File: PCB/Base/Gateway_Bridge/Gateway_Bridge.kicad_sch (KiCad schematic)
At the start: 57 parts, among them J1 J_DIAG, J2 J_I2C2, J3 STM32_Breakout, J5 J_CAN_TERM, J6 J_I2C1, J7 J_SWD, J8 J_BUS_IN, J9 J_BUS_OUT, SW1 RESET, U1 STM32F103C8Tx, U2 SN65HVD230, U3 AMS1117-3.3, U4 RP2040-ZERO, Y1 8MHz

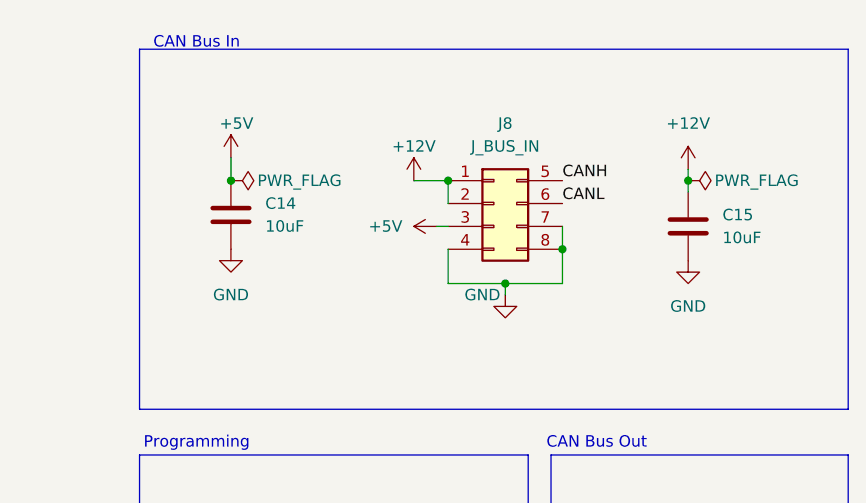
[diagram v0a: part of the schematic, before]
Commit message: feat(pcb): input-rail TVS + AO3400A backlight FET + 35V bus cap on base boards
Roll the #214 input-rail TVS fleet standard into both base boards, plus
two margin upgrades folded into the same rev:

- Input-rail TVS at J_BUS_IN on both boards: SMBJ12A (+12V, C42368008)
  and SMBJ6.0A (+5V, C5331096), cathode->rail / anode->GND, 2-3 GND
  vias at each anode pad for a low-inductance clamp path. CAN-bus TVS
  intentionally excluded (SN65HVD230 has built-in +/-16kV HBM).
- Backlight FET IRLML2502 -> AO3400A (C49195711, PanelGroup only):
  30V Vds vs 20V for headroom over the 19.9V clamp; Vgs operational at
  2.5V so still 3.3V-driven.
- +12V bulk cap C15 25V -> 35V X5R (C49010152): DC-bias derating +
  clamp headroom. C14 (+5V) stays 25V.

LCSC/MP/Voltage carried in-symbol. Combined BOM CSV + InvenTree updated.
DRC/ERC clean on both boards.

Refs #214
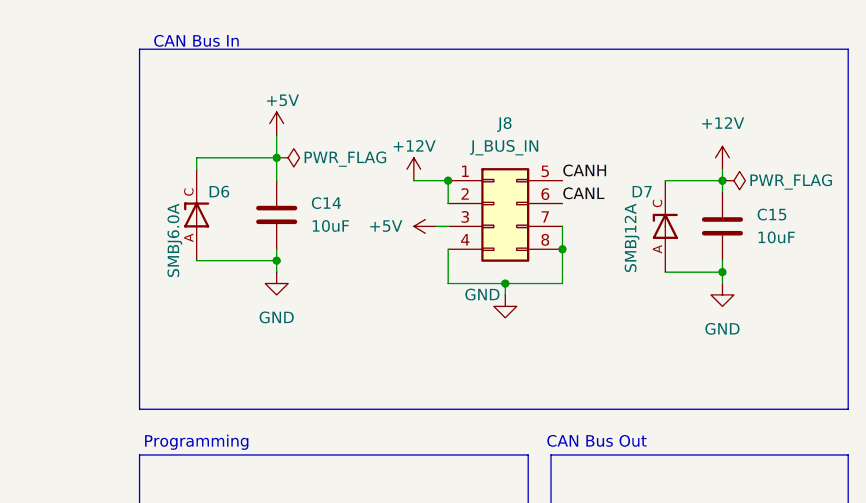
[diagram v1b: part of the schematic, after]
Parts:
- added D6: SMBJ6.0A, OpenSkyhawk:DIOM4336X265N, symbol OpenSkyhawk:SMBJ5.0A
- added D7: SMBJ12A, OpenSkyhawk:DIOM4336X265N, symbol OpenSkyhawk:SMBJ12A
- C15: LCSC (none) -> C49010152; Voltage (none) -> 35V
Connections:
- net +12V: now also D7.C
- net +5V: now also D6.C
- net GND: now also D6.A, D7.A
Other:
- moved on the sheet: C14, C15

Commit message: feat(pcb): label LCSC/tolerance/voltage across fleet boards (Right_Nav + PDU + base) (#235)
Populates **LCSC part number + tolerance + voltage** fields across all
six fleet boards, so each schematic drives an orderable BOM.

## Boards labeled (ERC 0/0 on all)
- **Right_Nav:** ASN-41, ARC-51A, APN-153
- **Power:** PDU
- **Base:** Gateway_Bridge, PanelGroup_Base

## What it does
- LCSC + tolerance + voltage on every assembled part, corrected to the
selected part (100nF 50V, resistors 1%, AMS1117 C6186→C347222, 10µF
split 25V/35V by +12V rail).
- Off-board panel controls (encoders, rotary switches, OLED, pot,
stepper, MEM button) left blank — connector-coupled, no assembly LCSC.
- Pin headers hand-soldered; RP2040-Zero left blank (module, sourced
separately).

## Design corrections captured here
- **PDU 1k series/anti-alias → 1%** (C110774 0.1% → C844939): precision
belongs only on the divider ratio resistors (33k/13k/10k); the series 1k
sit into high-Z ADC pins where 1% is identical. Drops the precision part
from the board.
- **DESIGN-NOTES:** records the 1k downgrade + the order-time shunt
upgrade (C346481 ±100ppm → C500740 ±25ppm, drop-in 2512).

## Not in this PR (follow-ups)
- Fleet component **standardization** (10µF-bulk→electrolytic,
consolidate to single 35V value, IPN convention) — separate pass.
- InvenTree backfill of the new SKUs.
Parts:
- C1: value 100nf -> 100nF; LCSC (none) -> C1711; Rating (none) -> 50V; Tolerance (none) -> 10%
- C10: LCSC (none) -> C28323; Rating (none) -> 50V; Tolerance (none) -> 10%
- C11: LCSC (none) -> C3343; Rating (none) -> 25V; Tolerance (none) -> 20%
- C12, C2, C3, C4, C5, C6, C9: LCSC (none) -> C1711; Rating (none) -> 50V; Tolerance (none) -> 10%
- C13: LCSC (none) -> C72502; Rating (none) -> 16V; Tolerance (none) -> 20%
- C14: value 10uF -> 100nF; LCSC (none) -> C1711; Rating (none) -> 50V; Tolerance (none) -> 10%
- C15: Rating (none) -> 35V; Tolerance (none) -> 20%
- C7, C8: LCSC (none) -> C1804; Rating (none) -> 50V; Tolerance (none) -> 5%
- D1, D3, D5: LCSC (none) -> C19171393
- D2, D4: LCSC (none) -> C19171391
- D6: Check_prices https://www.snapeda.com/parts/SMBJ5.0A/taiwan/view-part/?re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 -> (none); MF Taiwan Semiconductor -> MSKSEMI; PARTREV F2102 -> NA; Package SMD-2 Taiwan Semiconductor -> SMD-2; Purchase-URL https://www.snapeda.com/api/url_track_click_mouser/?unipart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 -> https://www.lcsc.com/product-detail/TVS_Diodes_MSKSEMI_SMBJ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; SnapEDA_Link https://www.snapeda.com/parts/SMBJ5.0A/taiwan/view-part/?re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 -> (none)
- D7: LCSC (none) -> C42368008; LCSV C42368008 -> (none)
- J1: LCSC (none) -> C51940188
- J2, J6: LCSC (none) -> C23067544
- J8, J9: LCSC (none) -> C20608116
- R1, R10, R7, R8, R9: LCSC (none) -> C844412; Rating (none) -> 1/8W; Tolerance (none) -> 1%
- R11, R12, R14, R15, R16, R17, R18: LCSC (none) -> C2090807; Rating (none) -> 1/8W; Tolerance (none) -> 1%
- R13: LCSC (none) -> C844816; Rating (none) -> 1/8W; Tolerance (none) -> 1%
- R2, R3, R4, R5: LCSC (none) -> C844941; Rating (none) -> 1/8W; Tolerance (none) -> 1%
- R6: LCSC (none) -> C844937; Rating (none) -> 1/8W; Tolerance (none) -> 1%
- R_BOOT1: value 10K -> 10k; LCSC (none) -> C844937; Rating (none) -> 1/8W; Tolerance (none) -> 1%
- SW1: LCSC (none) -> C2939600
- U1: LCSC (none) -> C8734
- U2: LCSC (none) -> C12084
- U3: LCSC (none) -> C347222
- Y1: LCSC (none) -> C20617997

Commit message: feat(pcb): add descriptive IPN field to all on-board symbols (#238 Phase 3) (#239)
Phase 3 of the IPN convention (#238): adds a stable, descriptive
**Internal Part Number** to every on-board symbol, co-equal with LCSC.
BOMs now anchor on a fixed identity; the LCSC can change with
availability without altering the part's identity.

## What changed
- **352 symbols** across all 6 boards (multi-sheet aware) get an `IPN`
field. **51 distinct IPNs.** ERC clean fleet-wide.
- **Off-board controls** (encoders/switches/pots/OLED/stepper — no
footprint, connector-coupled) get **no IPN**, per the standing off-board
exclusion. On-board modules (RP2040-ZERO) and the RESET tact switch
**do** get IPNs.
- `.gitignore`: FreeCAD backups (`*.FCBak`/`*.FCStd1`) + KiCad ERC/DRC
reports (`*-erc.rpt`/`*-drc.rpt`).

## Scheme (descriptive, locked in #238)
`RES-10K-1PCT-0805` · `CAP-CER-100NF-50V-0805` · `CAP-ELEC-22UF-16V-D4`
· `IC-STM32F103C8-LQFP` · `CONN-XH-8P` · `TVS-SMBJ12A-SMB` ·
`FUSE-HOLDER-BLADE-DIP4` · `SW-TACT-6MM` · `MOD-RP2040-ZERO`.

Resolved the 3 open encoding items: ferrite → `FB-600R-0805` (TDK
600Ω@100MHz), NTC → `NTC-10K-1206` (APV 10K), fuse holder (C19727305 is
a *holder*, not a fuse) → one `FUSE-HOLDER-BLADE-DIP4`.

## Not in this PR (later phases of #238)
- **Phase 2 — InvenTree:** set the IPN field + link SupplierParts incl
backorder alternates (one IPN → many LCSC). This is what actually
delivers the churn-proofing; needs reviewed InvenTree writes.
- **Phase 4 — order flow:** resolve IPN → in-stock LCSC at order time.

Refs #238.
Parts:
- C1, C12, C14, C2, C3, C4, C5, C6, C9: IPN (none) -> CAP-CER-100NF-50V-0805
- C10: IPN (none) -> CAP-CER-1UF-50V-0805
- C11: IPN (none) -> CAP-ELEC-10UF-25V-D4
- C13: IPN (none) -> CAP-ELEC-22UF-16V-D4
- C15: IPN (none) -> CAP-CER-10UF-35V-0805
- C7, C8: IPN (none) -> CAP-C0G-22PF-50V-0805
- D1, D3, D5: IPN (none) -> LED-GREEN-0805
- D2, D4: IPN (none) -> LED-RED-0805
- D6: IPN (none) -> TVS-SMBJ6V0A-SMB
- D7: IPN (none) -> TVS-SMBJ12A-SMB
- J1: IPN (none) -> CONN-XH-3P
- J2, J6: IPN (none) -> CONN-XH-4P
- J3: IPN (none) -> CONN-HDR-20P
- J5: IPN (none) -> CONN-HDR-2P
- J7: IPN (none) -> CONN-HDR-5P
- J8, J9: IPN (none) -> CONN-MF-8P
- R1, R10, R7, R8, R9: IPN (none) -> RES-3K3-1PCT-0805
- R11, R12, R14, R15, R16, R17, R18: IPN (none) -> RES-33R-1PCT-0805
- R13: IPN (none) -> RES-120R-1PCT-0805
- R2, R3, R4, R5: IPN (none) -> RES-4K7-1PCT-0805
- R6, R_BOOT1: IPN (none) -> RES-10K-1PCT-0805
- SW1: IPN (none) -> SW-TACT-6MM
- U1: IPN (none) -> IC-STM32F103C8-LQFP
- U2: IPN (none) -> IC-SN65HVD230-SOIC
- U3: IPN (none) -> IC-AMS1117-3V3-SOT223
- U4: IPN (none) -> MOD-RP2040-ZERO
- Y1: IPN (none) -> XTAL-8MHZ-SMD5032

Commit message: feat(pcb): +12V bulk cap → 22µF/35V electrolytic reroute (#236) (#243)
## What
Replaces the **+12V bulk cap** across ASN-41, PDU, Gateway_Bridge and
PanelGroup_Base:
**10µF/35V ceramic (0805) → 22µF/35V aluminium electrolytic**
`C48971029` (`Capacitor_SMD:CP_Elec_5x5.4`).

## Why (#236)
- 10µF/35V *ceramic* on a 12V rail DC-bias-derates to ~4–6µF;
electrolytic holds full value at ~1/5 the cost.
- Footprint grows 0805 → Ø5 (35V elec), so fabbed boards get a reroute;
value taken to 22µF (same Ø5 can) for margin.

## Changes
- Symbol fields updated: IPN `CAP-ELEC-22UF-35V-D5`, LCSC `C48971029`,
Rating `35V`, Tolerance `20%`.
- **PDU (C9), Gateway_Bridge (C15), PanelGroup_Base (C15)** — rerouted
for the Ø5 land; board revision **0.1.0 → 0.2.0**.
- **ASN-41 (C15)** — unrouted, schematic only; revision **0.1.0**.

## Verification
- ERC clean (0/0) on all four boards.
- CI (KiCad PR Reports) runs ERC/DRC.

Closes #236 — the +12V ceramic→electrolytic reroute was the
consolidation's last open action; the rest is decided and applied (per
#235 + this PR).
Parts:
- removed C15: 10uF, Capacitor_SMD:C_0805_2012Metric, symbol Device:C
- added C15: 22uF, Capacitor_SMD:CP_Elec_5x5.4, symbol Device:C_Polarized_Small
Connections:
- net +12V: now also C15.1
- net GND: now also C15.2

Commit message: fix(pcb): Gateway UART series resistors R16/R17 33 Ω → 1k
The RP2040 runs only from USB and the STM32 from the bus, so either can be
unpowered while the other drives an idle-high TX into it. With 33 Ω the
unpowered chip is back-fed through its ESD diode at tens of mA; 1k caps it at
~3 mA, with ~10 ns edge cost against a 4 µs bit at 250 kbaud.

Fields only (Value, IPN RES-1K-1PCT-0805, LCSC C844939): same 0805 footprint,
no layout change, stencil unaffected. ERC 0, DRC 0, schematic parity 0.
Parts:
- R16, R17: value 33 -> 1k; IPN RES-33R-1PCT-0805 -> RES-1K-1PCT-0805; LCSC C2090807 -> C844939
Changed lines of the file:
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@@
 			)
 		)
-		(property "Value" "33"
+		(property "Value" "1k"
 			(at 210.82 120.65 90)
 			(show_name no)
@@
 			)
 		)
-		(property "IPN" "RES-33R-1PCT-0805"
+		(property "IPN" "RES-1K-1PCT-0805"
 			(at 210.82 123.19 0)
 			(hide yes)
@@
 			)
 		)
-		(property "LCSC" "C2090807"
+		(property "LCSC" "C844939"
 			(at 210.82 123.19 0)
 			(hide yes)
@@
 			)
 		)
-		(property "Value" "33"
+		(property "Value" "1k"
 			(at 210.82 111.76 90)
 			(show_name no)
@@
 			)
 		)
-		(property "IPN" "RES-33R-1PCT-0805"
+		(property "IPN" "RES-1K-1PCT-0805"
 			(at 210.82 114.3 0)
 			(hide yes)
@@
 			)
 		)
-		(property "LCSC" "C2090807"
+		(property "LCSC" "C844939"
 			(at 210.82 114.3 0)
 			(hide yes)
